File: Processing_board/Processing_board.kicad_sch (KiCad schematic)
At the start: 30 parts, among them J1 Conn_01x08_Pin, J2 Conn_01x08_Pin, J3 Conn_01x06_Pin, J4 Conn_01x03_Pin, J5 Conn_01x03_Pin, J6 Conn_01x02_Pin, J7 Conn_01x02_Pin, SW1 TL3305BF100QG, SW2 TL3305BF100QG, U1 STM32WBA63CIU6

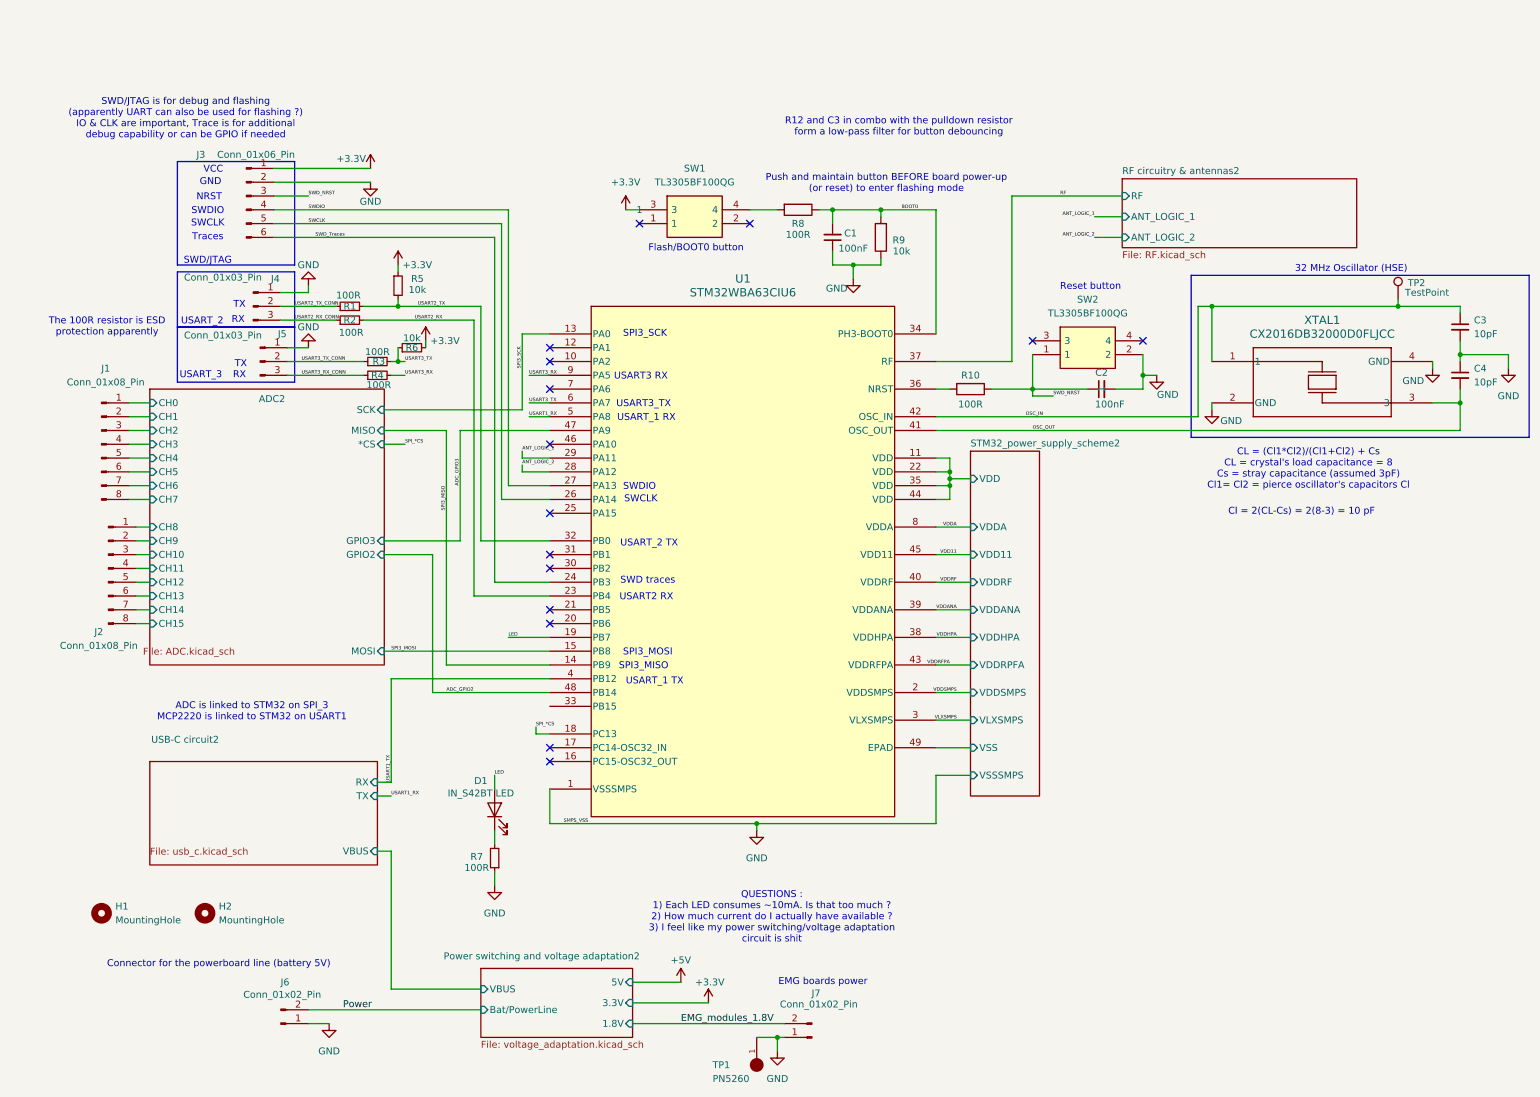
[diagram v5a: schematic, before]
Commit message: correct text height/width for silkscreen, correct 3D models for THT pin headers
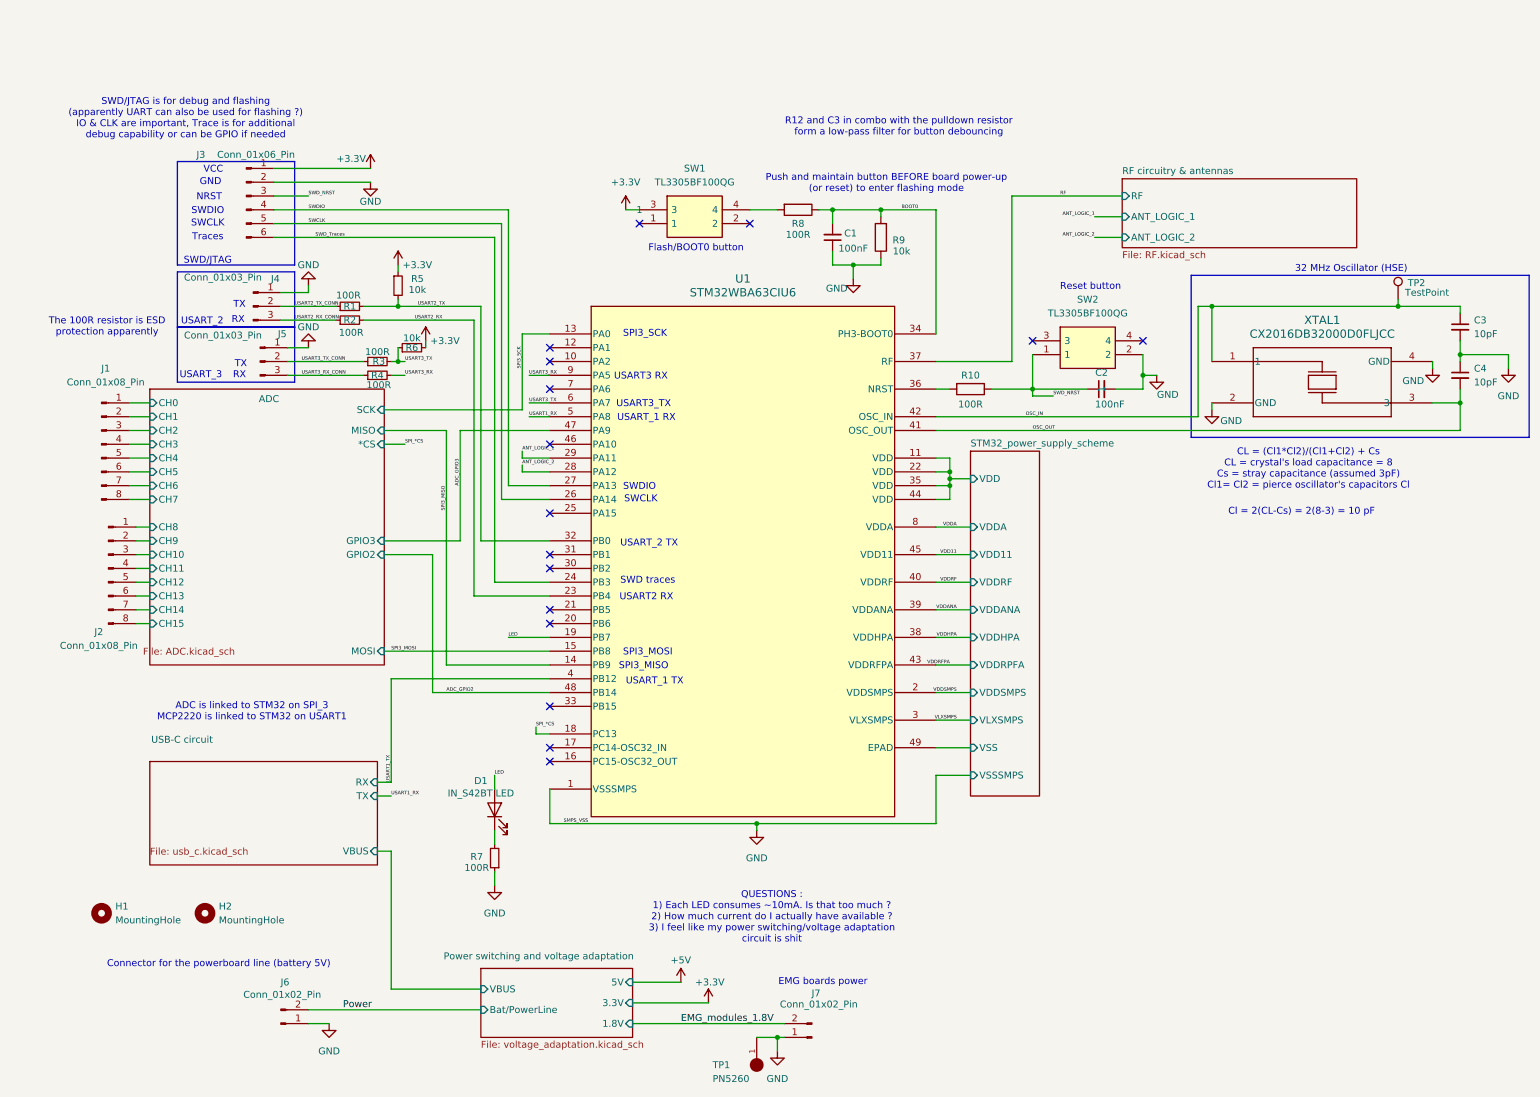
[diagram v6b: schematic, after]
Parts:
- J1, J2: footprint Connector_PinHeader_2.54mm:PinHeader_1x08_P2.54mm_Vertical_SMD_Pin1Left -> Connector_PinSocket_2.54mm:PinSocket_1x08_P2.54mm_Vertical
- J3: footprint Connector_PinHeader_2.54mm:PinHeader_1x06_P2.54mm_Vertical_SMD_Pin1Left -> Connector_PinSocket_2.54mm:PinSocket_1x06_P2.54mm_Vertical
- J4, J5: footprint Connector_PinHeader_2.54mm:PinHeader_1x03_P2.54mm_Vertical_SMD_Pin1Left -> Connector_PinSocket_2.54mm:PinSocket_1x03_P2.54mm_Vertical
- J6, J7: footprint Connector_PinHeader_2.54mm:PinHeader_1x02_P2.54mm_Vertical_SMD_Pin1Left -> Connector_PinSocket_2.54mm:PinSocket_1x02_P2.54mm_Vertical
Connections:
- no-connect marks 15 -> 16
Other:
- sheet ADC2 renamed ADC
- sheet Power switching and voltage adaptation2 renamed Power switching and voltage adaptation
- sheet RF circuitry & antennas2 renamed RF circuitry & antennas
- sheet STM32_power_supply_scheme2 renamed STM32_power_supply_scheme
- sheet USB-C circuit2 renamed USB-C circuit
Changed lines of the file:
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@@
 	)
 	(no_connect
+		(at 105.41 128.27)
+	)
+	(no_connect
 		(at 105.41 110.49)
 	)
@@
 			)
 		)
-		(property "Footprint" "Connector_PinHeader_2.54mm:PinHeader_1x06_P2.54mm_Vertical_SMD_Pin1Left"
+		(property "Footprint" "Connector_PinSocket_2.54mm:PinSocket_1x06_P2.54mm_Vertical"
 			(at 49.53 34.29 0)
 			(effects
@@
 			)
 		)
-		(property "Footprint" "Connector_PinHeader_2.54mm:PinHeader_1x02_P2.54mm_Vertical_SMD_Pin1Left"
+		(property "Footprint" "Connector_PinSocket_2.54mm:PinSocket_1x02_P2.54mm_Vertical"
 			(at 55.88 186.69 0)
 			(effects
@@
 			)
 		)
-		(property "Footprint" "Connector_PinHeader_2.54mm:PinHeader_1x02_P2.54mm_Vertical_SMD_Pin1Left"
+		(property "Footprint" "Connector_PinSocket_2.54mm:PinSocket_1x02_P2.54mm_Vertical"
 			(at 153.67 189.23 0)
 			(effects
@@
 			)
 		)
-		(property "Footprint" "Connector_PinHeader_2.54mm:PinHeader_1x03_P2.54mm_Vertical_SMD_Pin1Left"
+		(property "Footprint" "Connector_PinSocket_2.54mm:PinSocket_1x03_P2.54mm_Vertical"
 			(at 52.07 64.77 0)
 			(effects
@@
 			)
 		)
-		(property "Footprint" "Connector_PinHeader_2.54mm:PinHeader_1x08_P2.54mm_Vertical_SMD_Pin1Left"
+		(property "Footprint" "Connector_PinSocket_2.54mm:PinSocket_1x08_P2.54mm_Vertical"
 			(at 22.86 80.01 0)
 			(effects
@@
 			)
 		)
-		(property "Footprint" "Connector_PinHeader_2.54mm:PinHeader_1x08_P2.54mm_Vertical_SMD_Pin1Left"
+		(property "Footprint" "Connector_PinSocket_2.54mm:PinSocket_1x08_P2.54mm_Vertical"
 			(at 24.13 102.87 0)
 			(effects
@@
 			)
 		)
-		(property "Footprint" "Connector_PinHeader_2.54mm:PinHeader_1x03_P2.54mm_Vertical_SMD_Pin1Left"
+		(property "Footprint" "Connector_PinSocket_2.54mm:PinSocket_1x03_P2.54mm_Vertical"
 			(at 50.8 54.61 0)
 			(effects
@@
 			(color 0 0 0 0.0000)
 		)
-		(property "Sheetname" "ADC2"
+		(property "Sheetname" "ADC"
 			(at 51.816 72.39 0)
 			(effects
@@
 			(color 0 0 0 0.0000)
 		)
-		(property "Sheetname" "RF circuitry & antennas2"
+		(property "Sheetname" "RF circuitry & antennas"
 			(at 210.82 30.4034 0)
 			(effects
@@
 			(color 0 0 0 0.0000)
 		)
-		(property "Sheetname" "USB-C circuit2"
+		(property "Sheetname" "USB-C circuit"
 			(at 32.004 135.128 0)
 			(effects
@@
 			(color 0 0 0 0.0000)
 		)
-		(property "Sheetname" "STM32_power_supply_scheme2"
+		(property "Sheetname" "STM32_power_supply_scheme"
 			(at 182.88 80.5684 0)
 			(effects
@@
 			(color 0 0 0 0.0000)
 		)
-		(property "Sheetname" "Power switching and voltage adaptation2"
+		(property "Sheetname" "Power switching and voltage adaptation"
 			(at 85.852 175.006 0)
 			(effects

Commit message: last changes before ordering
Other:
- sheet USB-C circuit ports: added MCP2200_RX, MCP2200_TX; removed RX, TX
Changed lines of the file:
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@@
 			)
 		)
-		(pin "RX" input
+		(pin "MCP2200_RX" input
 			(at 73.66 142.24 0)
 			(effects
@@
 			)
 		)
-		(pin "TX" input
+		(pin "MCP2200_TX" input
 			(at 73.66 144.78 0)
 			(effects

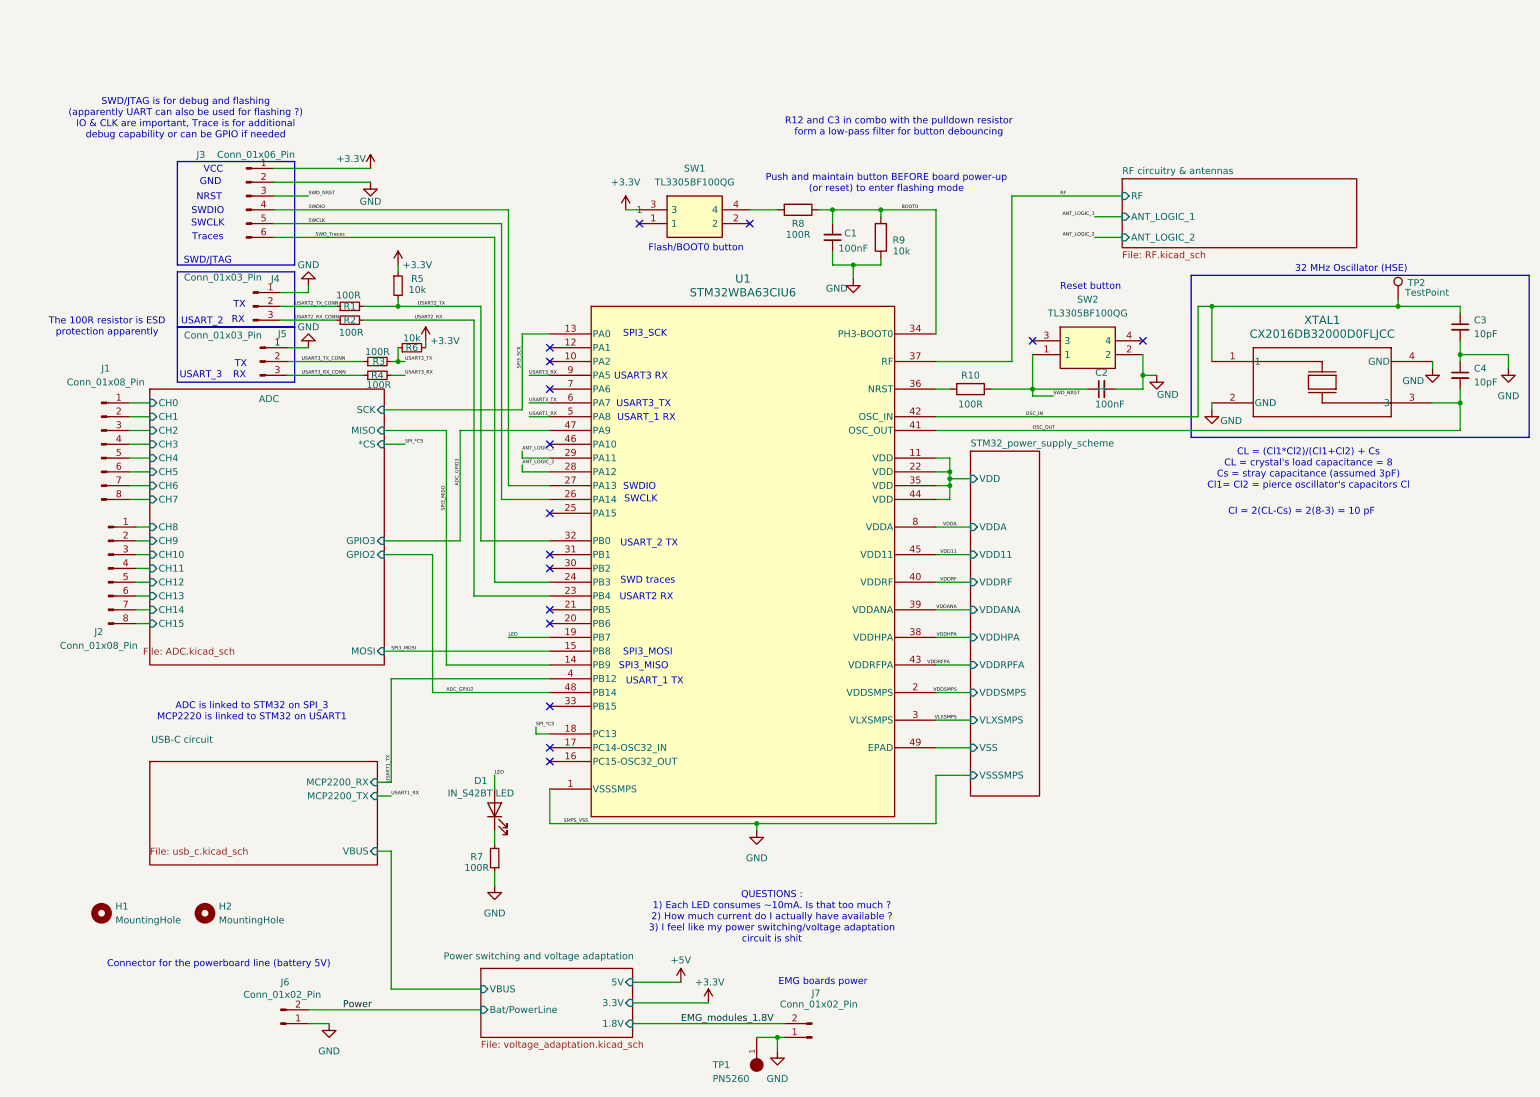
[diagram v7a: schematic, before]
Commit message: added Block Diagram (in KiCad and PDF) ; minor silkscreen cleanup
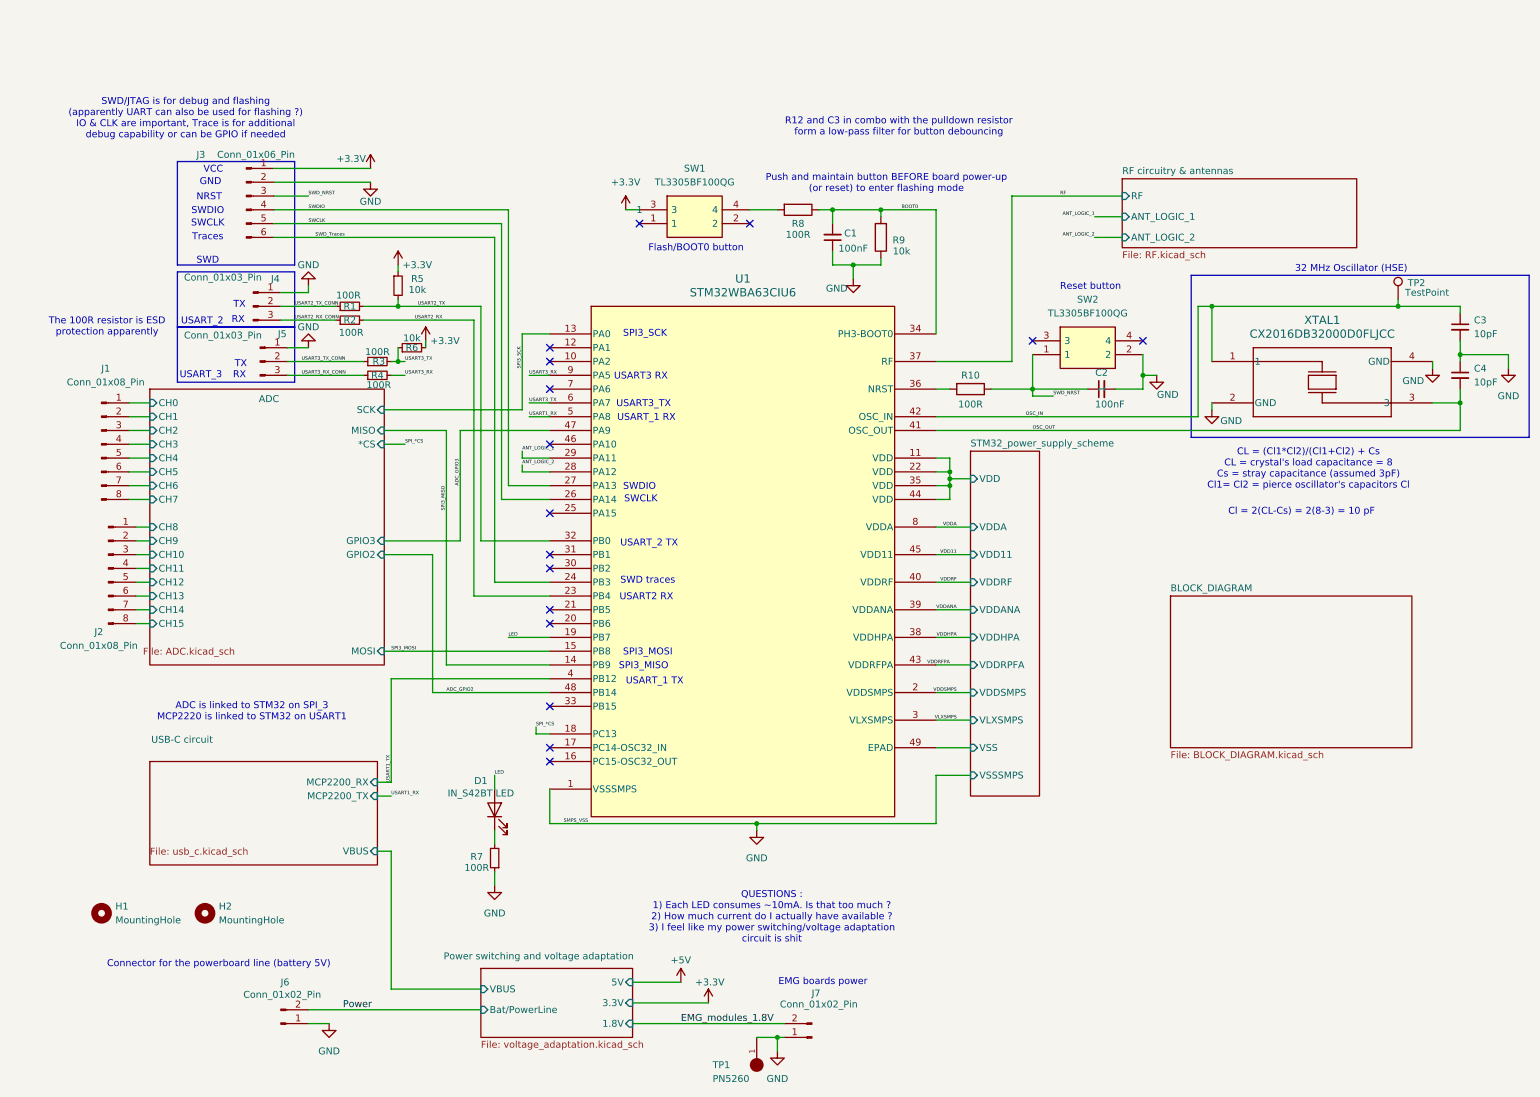
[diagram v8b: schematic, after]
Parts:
- C1, C2: Link https://www.mouser.ch/ProductDetail/Samsung-Electro-Mechani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 -> https://eu.mouser.com/ProductDetail/Samsung-Electro-Mechani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; Manufacturer_Part_Number CL05B104KP5VPNC -> CL05B104KP5VPNC
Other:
- added sheet BLOCK_DIAGRAM (BLOCK_DIAGRAM.kicad_sch)
- note added: "SWD"
- note removed: "SWD/JTAG"
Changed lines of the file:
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@@
 		)
 	)
-	(text "SWD/JTAG"
+	(text "SWD"
 		(exclude_from_sim no)
 		(at 42.418 46.228 0)
@@
 			)
 		)
-		(property "Link" "https://www.mouser.ch/ProductDetail/Samsung-Electro-Mechanics/CL05B104KP5VPNC?qs=gqBM4hNBiUXTv%252BkFO9q2pQ%3D%3D"
+		(property "Link" "https://eu.mouser.com/ProductDetail/Samsung-Electro-Mechanics/CL05B104KP5VPNC?qs=gqBM4hNBiUXTv%252BkFO9q2pQ%3D%3D"
 			(at 207.01 69.85 0)
 			(effects
@@
 			)
 		)
-		(property "Manufacturer_Part_Number" "CL05B104KP5VPNC"
+		(property "Manufacturer_Part_Number" "CL05B104KP5VPNC "
 			(at 207.01 69.85 0)
 			(effects
@@
 			)
 		)
-		(property "Link" "https://www.mouser.ch/ProductDetail/Samsung-Electro-Mechanics/CL05B104KP5VPNC?qs=gqBM4hNBiUXTv%252BkFO9q2pQ%3D%3D"
+		(property "Link" "https://eu.mouser.com/ProductDetail/Samsung-Electro-Mechanics/CL05B104KP5VPNC?qs=gqBM4hNBiUXTv%252BkFO9q2pQ%3D%3D"
 			(at 157.48 41.91 0)
 			(effects
@@
 			)
 		)
-		(property "Manufacturer_Part_Number" "CL05B104KP5VPNC"
+		(property "Manufacturer_Part_Number" "CL05B104KP5VPNC "
 			(at 157.48 41.91 0)
 			(effects
@@
 				)
 			)
+		)
+	)
+	(sheet
+		(at 219.71 107.95)
+		(size 44.45 27.94)
+		(exclude_from_sim no)
+		(in_bom yes)
+		(on_board yes)
+		(dnp no)
+		(fields_autoplaced yes)
+		(stroke
+			(width 0.1524)
+			(type solid)
+		)
+		(fill
+			(color 86 116 255 1.0000)
+		)
+		(property "Sheetname" "BLOCK_DIAGRAM"
+			(at 219.71 107.2384 0)
+			(effects
+				(font
+					(size 1.27 1.27)
+				)
+				(justify left bottom)
+			)
+		)
+		(property "Sheetfile" "BLOCK_DIAGRAM.kicad_sch"
+			(at 219.71 136.4746 0)
+			(effects
+				(font
+					(size 1.27 1.27)
+				)
+				(justify left top)
+			)
+		)
+		(instances
+			(project "Processing_board"
+				(path "/b48cfd4a-6c36-4270-b2b4-45cb26e35477"
+					(page "7")
+				)
+			)
